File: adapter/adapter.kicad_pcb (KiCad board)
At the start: 2 copper layers, 96 x 18 mm, 26 parts, among them J1 MALE, J11 MALE, J12 FEMALE, J13 STANDOFF, J14 STANDOFF, J15 STANDOFF, J2 FEMALE, J3 STANDOFF, J4 STANDOFF, J5 STANDOFF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

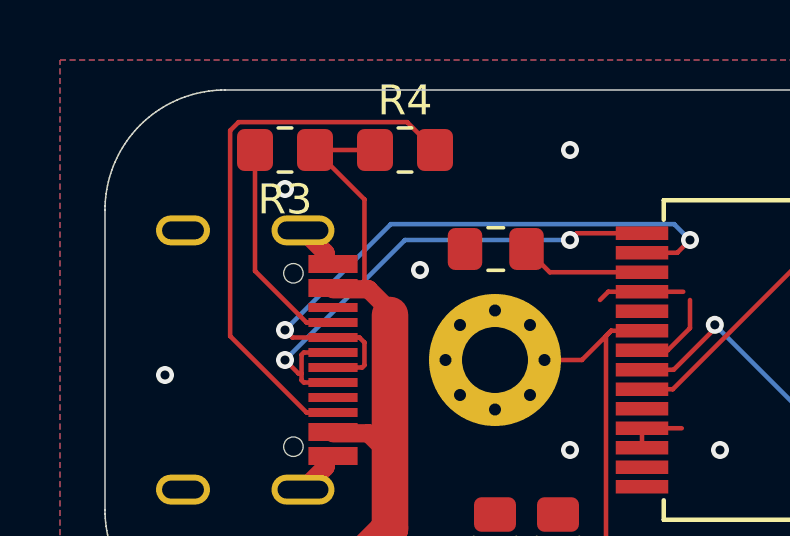
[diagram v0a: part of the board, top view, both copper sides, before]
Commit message: Reroute to reflect fix
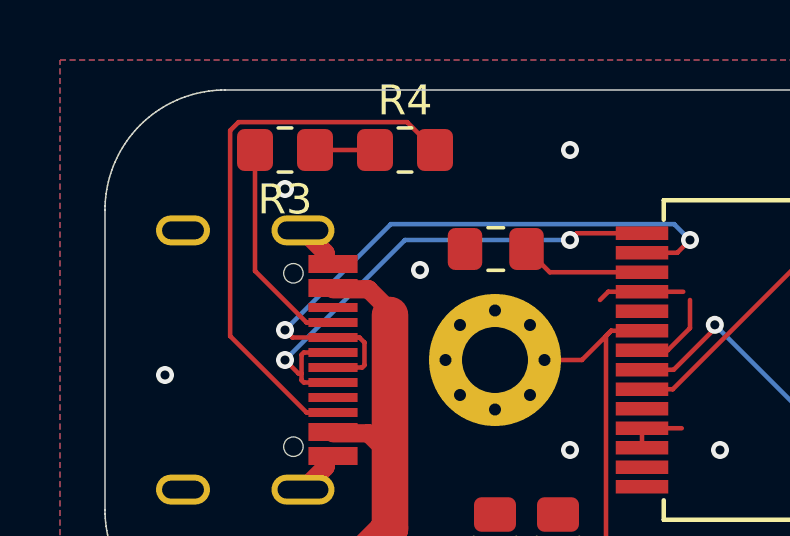
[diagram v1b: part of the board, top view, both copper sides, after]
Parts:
- R3, R4: value 56k -> 5.1k
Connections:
- R3 pad 1: /Lower Board/VBUS -> GNDB
- R4 pad 1: /Lower Board/VBUS -> GNDB
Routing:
- net /Lower Board/VBUS: track 27.3 -> 19.1 mm
- net GNDB: track 12.1 -> 14.4 mm

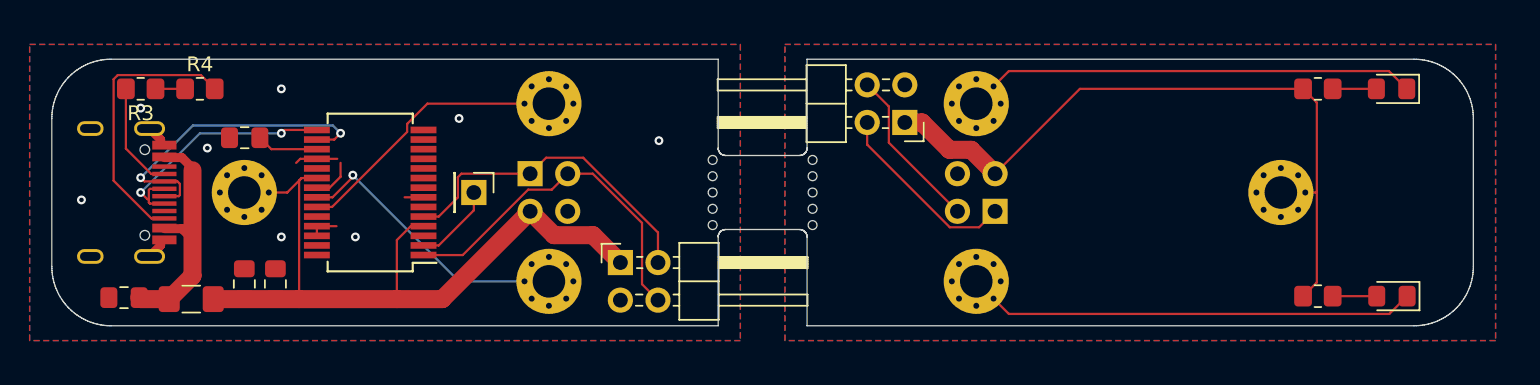
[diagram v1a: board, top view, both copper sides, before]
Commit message: Fix pinout
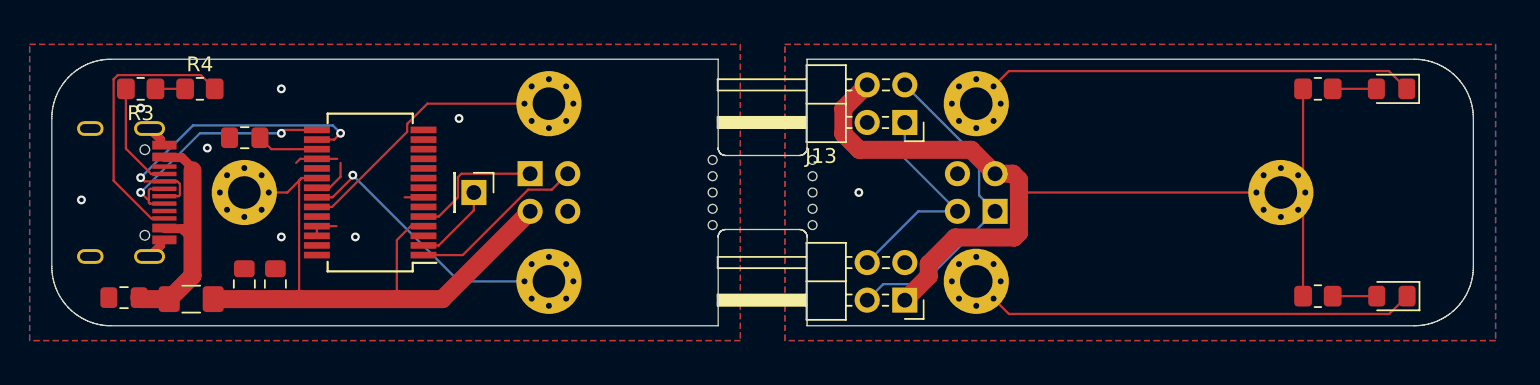
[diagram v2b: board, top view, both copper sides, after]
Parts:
- removed J1: MALE, Connector_PinHeader_2.54mm:PinHeader_2x02_P2.54mm_Horizontal
- added J13: MALE, Connector_PinHeader_2.54mm:PinHeader_2x02_P2.54mm_Horizontal, F.Cu at (158.1, 100.3)
- R3, R4: value 5.1k -> 56k
- moved J11 12.0 mm to (158.1, 112.3)
- renumbered J13 to J14, J14 to J15, J15 to J16
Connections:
- R3 pad 1: GNDB -> /Lower Board/VBUS
- R4 pad 1: GNDB -> /Lower Board/VBUS
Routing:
- net +5V: track 47.9 -> 63.8 mm
- net /Lower Board/RXD: track 22.4 -> 9.20 mm
- net /Lower Board/TXD: track 24.1 -> 12.0 mm
- net Net-(J11-Pad2): track 12.9 -> 22.2 mm
- net +5VB: track 51.1 -> 43.6 mm
- net Net-(J11-Pad4): track 11.1 -> 15.0 mm
- net GNDB: track 14.4 -> 12.1 mm, vias 8 -> 7
- net /Lower Board/VBUS: track 19.1 -> 21.4 mm
- net GND: vias 0 -> 1

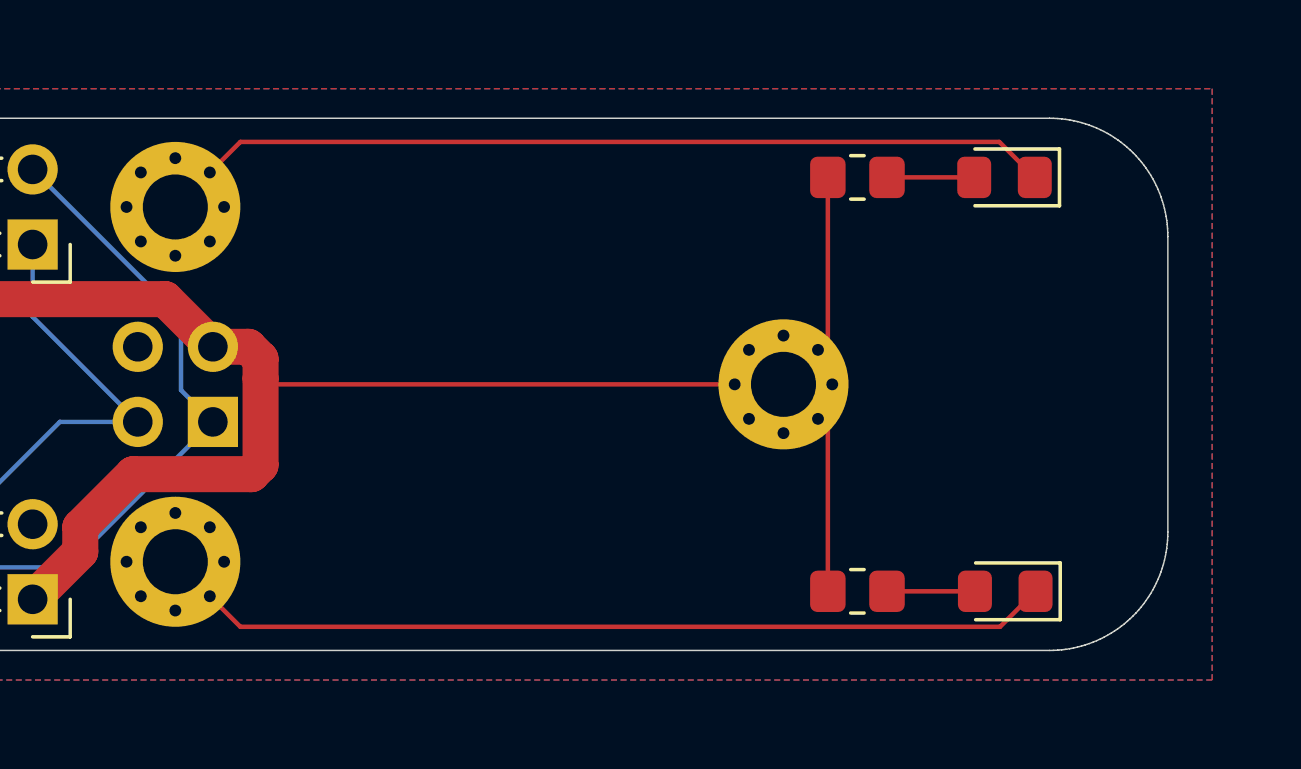
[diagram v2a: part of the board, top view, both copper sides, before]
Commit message: Add copper pour for aesthetic reasons
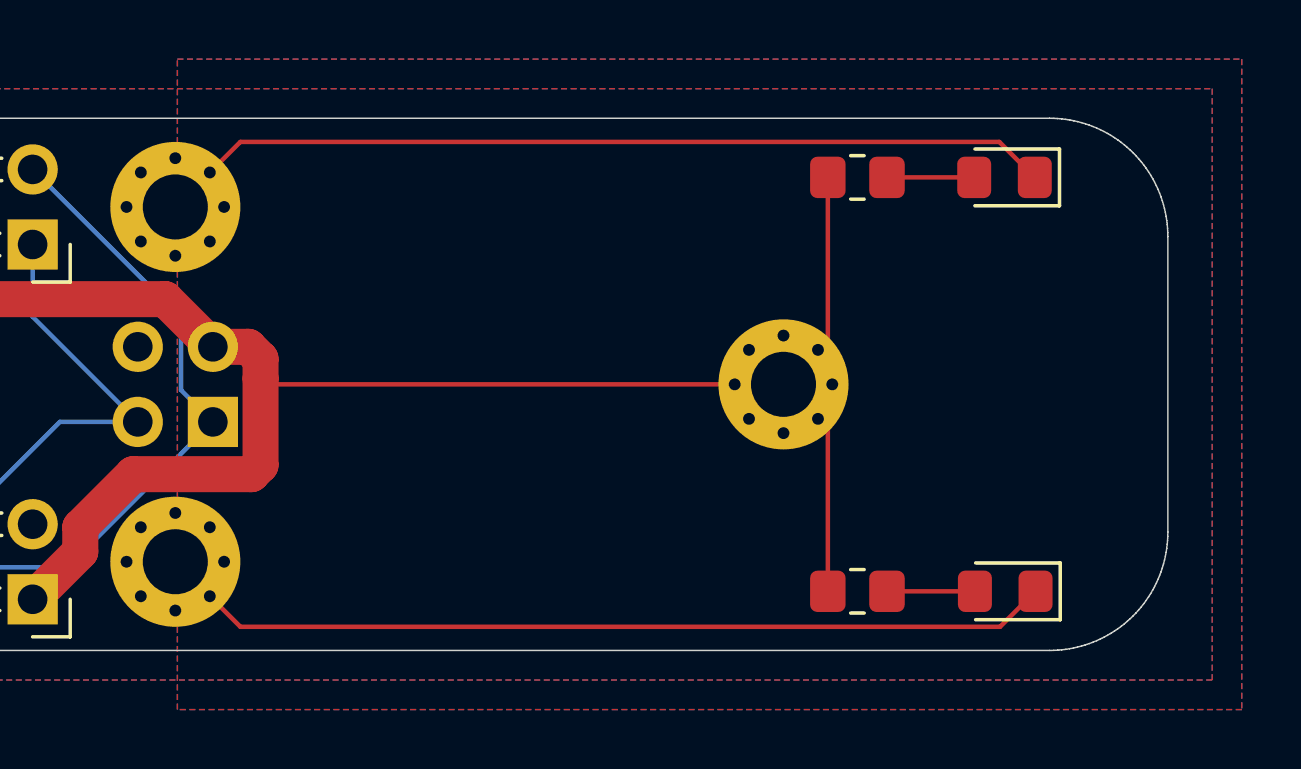
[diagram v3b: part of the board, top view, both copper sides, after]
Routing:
- added copper zone on B.Cu, net (none)
- added copper zone on F.Cu, net (none)

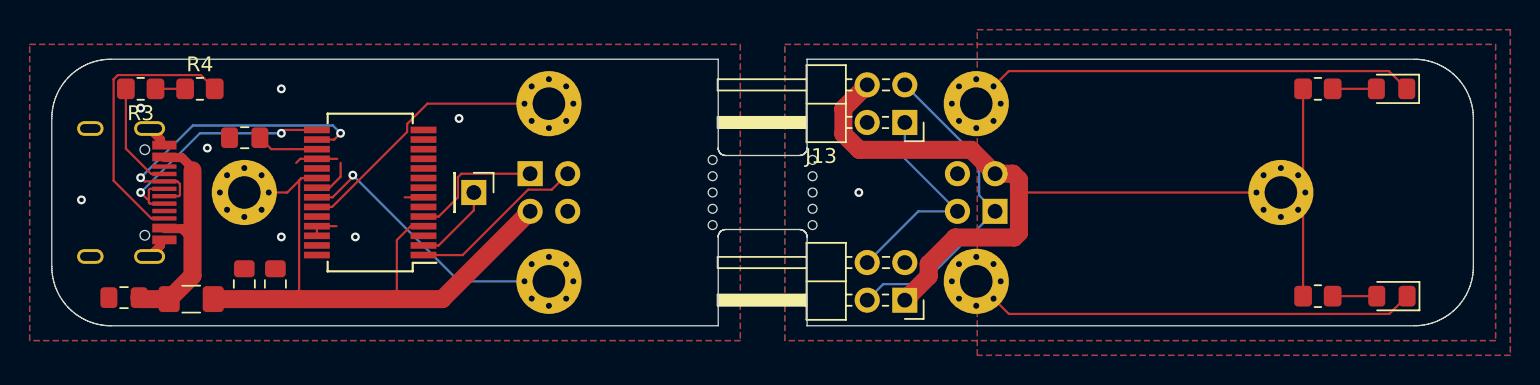
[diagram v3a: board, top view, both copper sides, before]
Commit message: Fix: USB-C port no configured as downstream
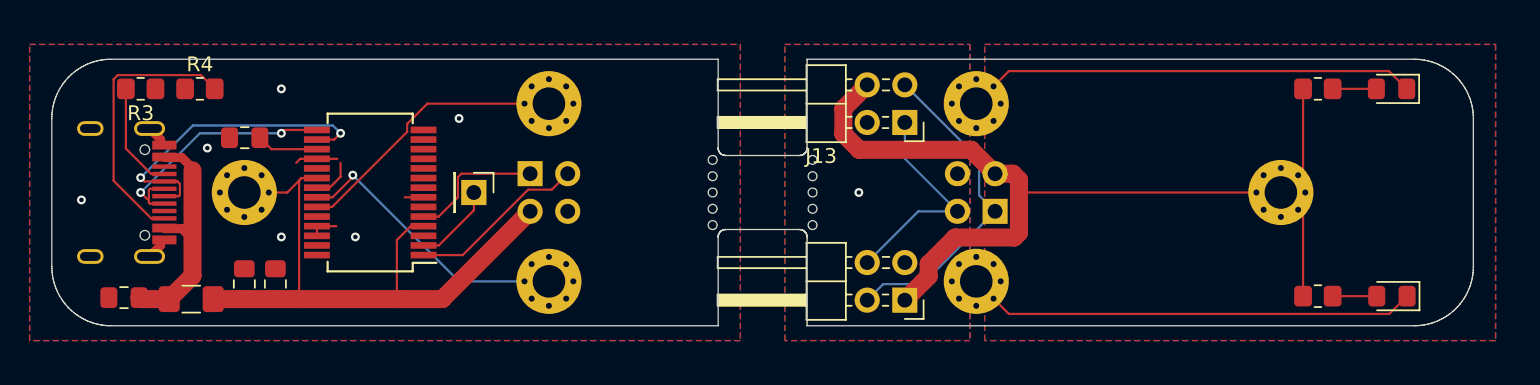
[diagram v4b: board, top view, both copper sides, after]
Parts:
- R3, R4: value 56k -> 5.1k
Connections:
- R3 pad 1: /Lower Board/VBUS -> GNDB
- R4 pad 1: /Lower Board/VBUS -> GNDB
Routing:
- net /Lower Board/VBUS: track 21.4 -> 19.1 mm
- net GNDB: track 12.1 -> 12.4 mm, vias 7 -> 6
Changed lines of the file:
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@@
     (thickness 1.6)
     (drawings 392)
-    (tracks 148)
+    (tracks 146)
     (zones 0)
     (modules 26)
@@
       (effects (font (size 1 1) (thickness 0.15)))
     )
-    (fp_text value 56k (at -0.1 1.7) (layer F.Fab)
+    (fp_text value 5.1k (at -0.1 1.7) (layer F.Fab)
       (effects (font (size 1 1) (thickness 0.15)))
     )
@@
       (net 29 "Net-(J6-PadA5)"))
     (pad 1 smd roundrect (at -1 0 180) (size 1.2 1.4) (layers F.Cu F.Paste F.Mask) (roundrect_rratio 0.208333)
-      (net 1 "/Lower Board/VBUS"))
+      (net 33 GNDB))
     (model ${KISYS3DMOD}/Resistor_SMD.3dshapes/R_0805_2012Metric.wrl
       (at (xyz 0 0 0))
@@
       (effects (font (size 1 1) (thickness 0.15)))
     )
-    (fp_text value 56k (at 0 -1.7) (layer F.Fab)
+    (fp_text value 5.1k (at 0 -1.7) (layer F.Fab)
       (effects (font (size 1 1) (thickness 0.15)))
     )
@@
       (net 28 "Net-(J6-PadB5)"))
     (pad 1 smd roundrect (at -1 0) (size 1.2 1.4) (layers F.Cu F.Paste F.Mask) (roundrect_rratio 0.208333)
-      (net 1 "/Lower Board/VBUS"))
+      (net 33 GNDB))
     (model ${KISYS3DMOD}/Resistor_SMD.3dshapes/R_0805_2012Metric.wrl
       (at (xyz 0 0 0))
@@
   (segment (start 110 103.357038) (end 109.285761 102.642799) (width 0.6096) (layer F.Cu) (net 1))
   (segment (start 110 103.5) (end 110 103.357038) (width 0.6096) (layer F.Cu) (net 1))
-  (segment (start 107.5 98) (end 109.5 98) (width 0.1524) (layer F.Cu) (net 1))
-  (segment (start 107.5 98) (end 107.5 98.3) (width 0.1524) (layer F.Cu) (net 1))
+  (segment (start 107.5 98) (end 107.5 98.3) (width 0.1524) (layer F.Cu) (net 33))
   (via (at 155 105) (size 0.6) (drill 0.3) (layers F.Cu B.Cu) (net 2))
   (segment (start 115.325 102.075) (end 118.4 102.075) (width 0.1524) (layer F.Cu) (net 3))
@@
   (segment (start 108.1 101.65) (end 108.1 101.95) (width 0.1524) (layer F.Cu) (net 33))
   (segment (start 108.1 108.05) (end 108.1 108.35) (width 0.1524) (layer F.Cu) (net 33))
-  (via (at 106.5 99.3) (size 0.6) (drill 0.3) (layers F.Cu B.Cu) (net 33))
   (segment (start 132.8 106.27) (end 126.87 112.2) (width 1.2192) (layer F.Cu) (net 34))
   (segment (start 117.2 104.1976) (end 117.2 112.2) (width 0.1524) (layer F.Cu) (net 34))
@@
     (polygon
       (pts
-        (xy 198 115) (xy 150 115) (xy 150 95) (xy 198 95)
+        (xy 162.5 115) (xy 150 115) (xy 150 95) (xy 162.5 95)
       )
     )
@@
     (polygon
       (pts
-        (xy 198 115) (xy 150 115) (xy 150 95) (xy 198 95)
+        (xy 162.5 115) (xy 150 115) (xy 150 95) (xy 162.5 95)
       )
     )
@@
     (polygon
       (pts
-        (xy 199 116) (xy 163 116) (xy 163 94) (xy 199 94)
+        (xy 198 115) (xy 163.5 115) (xy 163.5 95) (xy 198 95)
       )
     )
@@
     (polygon
       (pts
-        (xy 199 116) (xy 163 116) (xy 163 94) (xy 199 94)
+        (xy 198 115) (xy 163.5 115) (xy 163.5 95) (xy 198 95)
       )
     )

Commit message: Remove complicated zones on side not visible
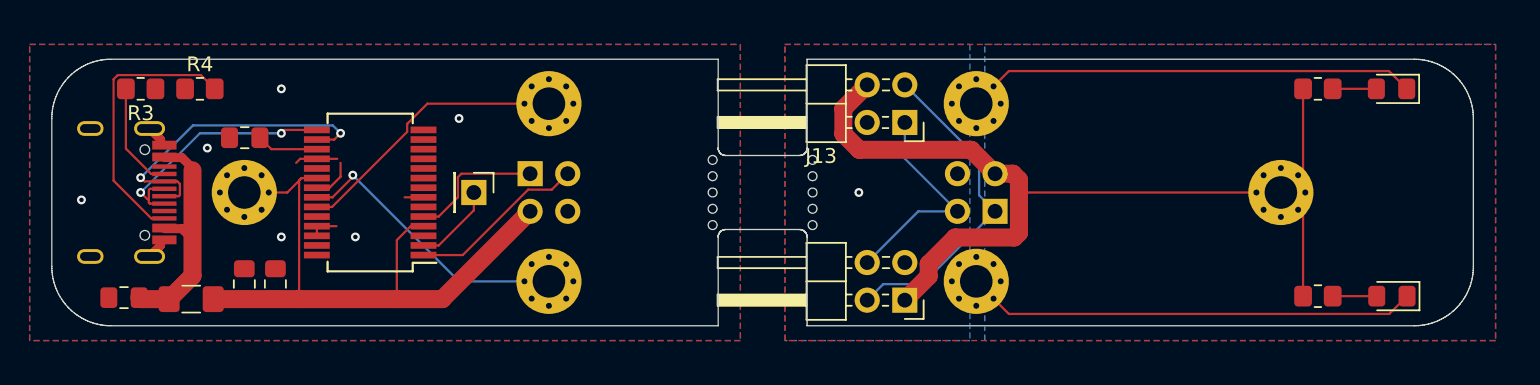
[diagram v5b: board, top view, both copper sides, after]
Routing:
- removed copper zone on F.Cu, net (none)
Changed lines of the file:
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@@
     (polygon
       (pts
-        (xy 162.5 115) (xy 150 115) (xy 150 95) (xy 162.5 95)
+        (xy 198 115) (xy 150 115) (xy 150 95) (xy 198 95)
       )
     )
@@
       )
     )
-  )
-  (zone (net 0) (net_name "") (layer F.Cu) (hatch edge 0.508)
-    (connect_pads (clearance 0.508))
-    (min_thickness 0.254)
-    (fill yes (arc_segments 32) (thermal_gap 0.508) (thermal_bridge_width 0.508))
-    (polygon
-      (pts
-        (xy 198 115) (xy 163.5 115) (xy 163.5 95) (xy 198 95)
-      )
-    )

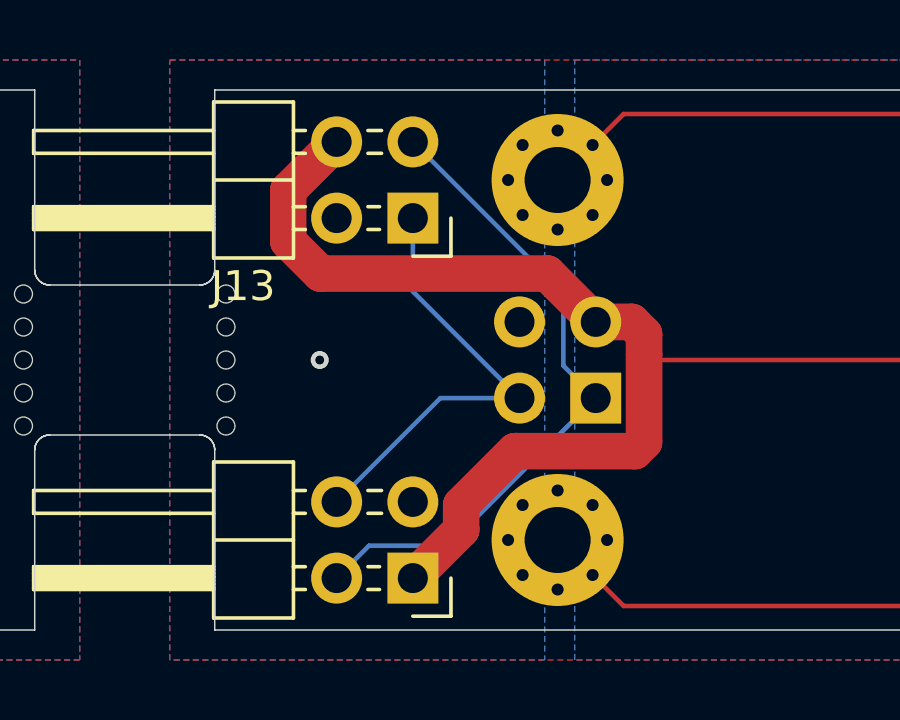
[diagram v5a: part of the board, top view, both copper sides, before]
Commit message: Rewire to match schematic
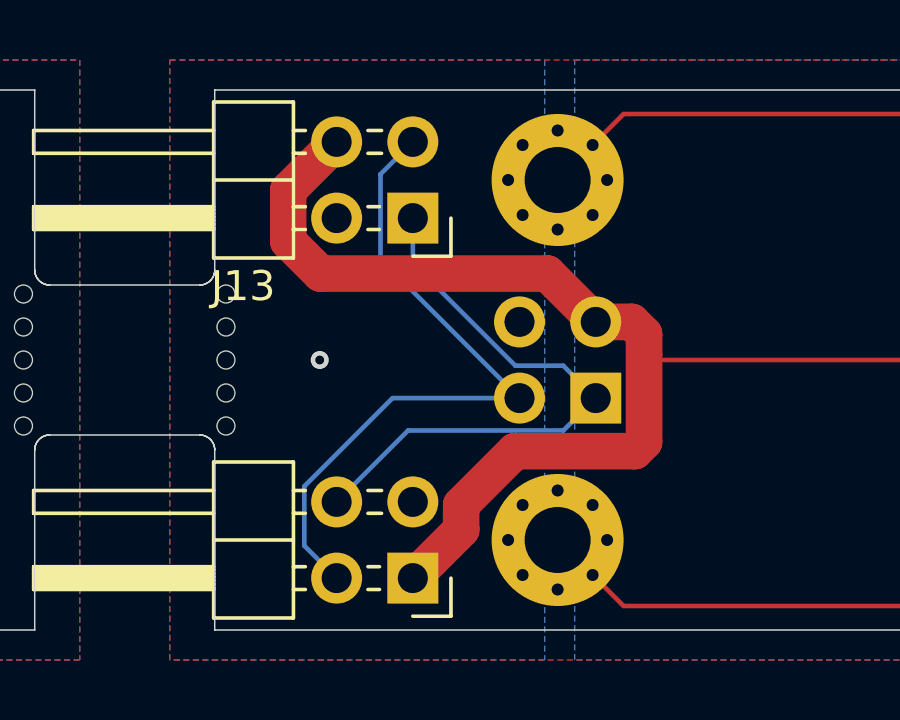
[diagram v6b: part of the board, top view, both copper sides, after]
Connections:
- J11 pad 2: Net-(J11-Pad2) -> /Upper Board/RX1T
- J11 pad 4: Net-(J11-Pad4) -> /Upper Board/TX1T
- J12 pad 1: Net-(J11-Pad2) -> /Upper Board/TX1T
- J12 pad 2: Net-(J11-Pad4) -> /Upper Board/RX1T
- J13 pad 1: Net-(J11-Pad4) -> /Upper Board/TX1T
- J13 pad 3: Net-(J11-Pad2) -> /Upper Board/RX1T
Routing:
- net /Upper Board/RX1T: track 0.00 -> 22.8 mm
- net Net-(J11-Pad2): track 22.2 -> 0.00 mm
- net /Upper Board/TX1T: track 0.00 -> 19.5 mm
- net Net-(J11-Pad4): track 15.0 -> 0.00 mm
